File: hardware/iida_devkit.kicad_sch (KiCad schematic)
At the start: 45 parts, among them J1 PRPC005DAAN-RC, J2 Tag-Connect TC2050, J3 Conn_01x02, J4 USB4085-GF-A, U1 STM32L552CEU6, U2 MX25U4035FM1I, U3 MCP9808, U4 USBLC6-2SC6, Y1 ABS05-32.768KHZ-9-T, Y2 ECS-160-9-37-CKM-TR3

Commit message: Start working on hw v4.0.0
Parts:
- removed C1, C2, C3, C4: 8 pF, perfect_footprints:0402_1005_perfect, symbol Device:C
- removed C5, C8: 100 nF, perfect_footprints:0402_1005_perfect, symbol Device:C
- removed C6: 4.7 µF, Capacitor_SMD:C_0603_1608Metric, symbol Device:C
- removed C7: 33 pF, perfect_footprints:0402_1005_perfect, symbol Device:C
- removed F1: 5A, Fuse:Fuse_1812_4532Metric, symbol Device:Polyfuse
- removed J1: PRPC005DAAN-RC, Connector_PinHeader_2.54mm:PinHeader_2x05_P2.54mm_Vertical, symbol Connector_Generic:Conn_02x05_Odd_Even
- removed J2: Tag-Connect TC2050, Connector:Tag-Connect_TC2050-IDC-FP_2x05_P1.27mm_Vertical, symbol Connector:Conn_ARM_JTAG_SWD_10
- removed J3: Conn_01x02, Connector_PinHeader_2.54mm:PinHeader_1x02_P2.54mm_Vertical, symbol Connector_Generic:Conn_01x02
- removed J4: USB4085-GF-A, USB4105-GF-A:USB4085-GF-A, symbol USB4085-GF-A:USB4085-GF-A
- removed LED1, LED2, LED3, LED4: LS T67K-K1L2-1-0-2-R18-Z, LED_SMD:LED_PLCC_2835, symbol Device:LED
- removed R1, R2, R3, R4, R5, R6: 2.2 kΩ, perfect_footprints:0402_1005_perfect, symbol Device:R
- removed R10, R11, R12, R9: 0 Ω, perfect_footprints:0402_1005_perfect, symbol Device:R
- removed R13, R14: 5.1 kΩ, perfect_footprints:0402_1005_perfect, symbol Device:R
- removed R7, R8: 10 kΩ, perfect_footprints:0402_1005_perfect, symbol Device:R
- removed SW_SPST1: SW_RESET, Button_Switch_SMD:SW_SPST_PTS645, symbol Switch:SW_SPST
- removed U1: STM32L552CEU6, Package_DFN_QFN:QFN-48-1EP_7x7mm_P0.5mm_EP5.6x5.6mm, symbol MCU_ST_STM32L5:STM32L552CEUx
- removed U2: MX25U4035FM1I, Package_SO:SOIC-8_3.9x4.9mm_P1.27mm, symbol MX25U4035FM1I:MX25U4035FM1I
- removed U3: MCP9808, Package_SO:MSOP-8_3x3mm_P0.65mm, symbol Sensor_Temperature:MCP9808_MSOP
- removed U4: USBLC6-2SC6, Package_TO_SOT_SMD:SOT-23-6, symbol Power_Protection:USBLC6-2SC6
- removed Y1: ABS05-32.768KHZ-9-T, Crystal:Crystal_SMD_MicroCrystal_CM9V-T1A-2Pin_1.6x1.0mm, symbol Device:Crystal
- removed Y2: ECS-160-9-37-CKM-TR3, Crystal:Crystal_SMD_2016-4Pin_2.0x1.6mm, symbol Device:Crystal_GND24
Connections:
- no-connect marks 9 -> 0
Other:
- added sheet MCU (mcu.kicad_sch)
- note added: "Ext flash"
- note added: "Modem"
- note added: "POWER"
- note added: "SIM"
- note added: "Temp sensor"
- note removed: "16 MHz"
- note removed: "32.768 kHz"
- note removed: "Crystals"
- note removed: "Debug LEDs"
- note removed: "External flash"
- note removed: "Fiducial markers"
- note removed: "Hardware ID map"
- note removed: "Mounting holes"
- note removed: "NOTE: STM32F446RET6 has an internal pull-up resistor for D+"
- note removed: "Peripheral debug"
- note removed: "Programming header"
- note removed: "Reset"
- note removed: "Temperature sensor"
- note removed: "USB"
- note removed: "USBLC6-2 Datasheet: 1: D+ in 2: GND 3: D- in 4: D- out 5: VBUS 6: D+ out"
- note removed: "Wakeup"
- note removed: "With A0 .. A2 tied to ground, the address is 0b001'1000 (=0x18h)."

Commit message: HW: Develop further
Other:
- added sheet SIM (sim.kicad_sch)
- sheet MCU ports: added +3.3VA_MCU, +3.3V_MCU, MODEM_RX, MODEM_TX, ~{MODEM_PWR_EN}, ~{MODEM_RESET}; removed none
- sheet Modem ports: added +3.3V_MDM, MODEM_RX, MODEM_TX, SIM_CLK, SIM_IO, SIM_RST, VSIM, ~{MODEM_RESET}; removed none
- sheet Power ports: added +3.3VA_MCU, +3.3V_MCU, +3.3V_MDM, ~{MODEM_PWR_EN}; removed none
- note added: "Place fiducial markers at each (-1) corner of the PCB."
- note added: "Place mounting holes at the four corners of the PCB."
- note removed: "Ext flash"
- note removed: "MCU"
- note removed: "Modem"
- note removed: "POWER"
- note removed: "SIM"
- note removed: "Temp sensor"
- moved on the sheet: FID1, FID2, FID3, H1, H2, H3, H4

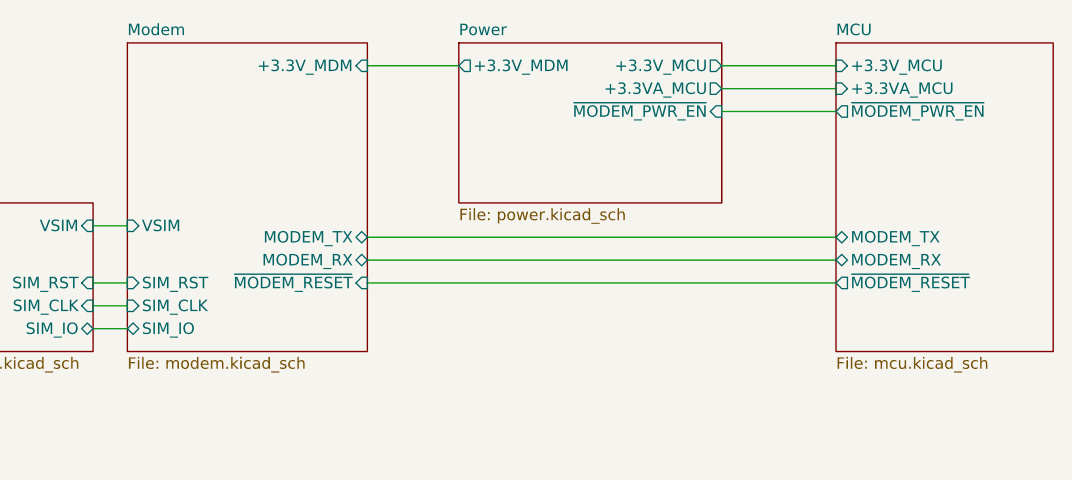
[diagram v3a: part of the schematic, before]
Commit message: HW: Rework power section
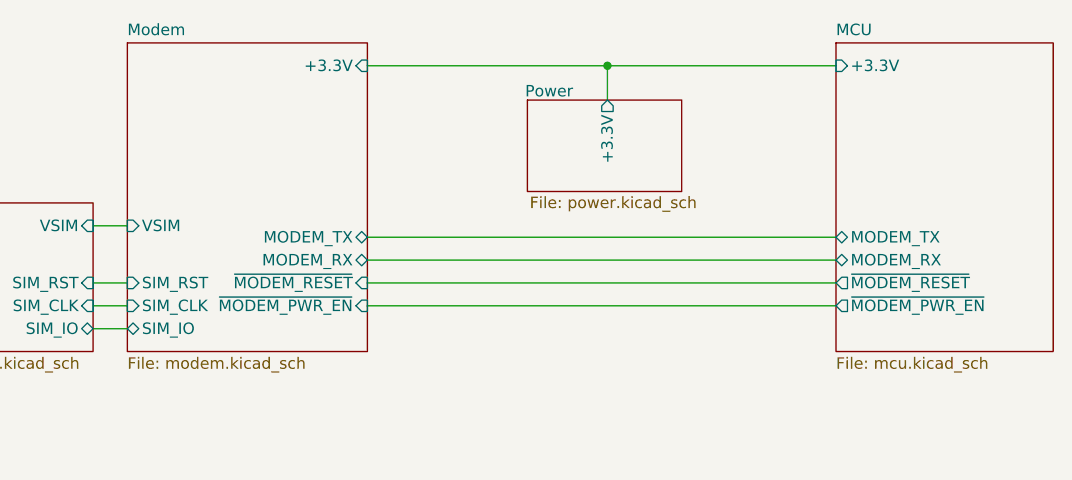
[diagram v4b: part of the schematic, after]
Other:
- sheet MCU ports: added +3.3V; removed +3.3VA_MCU, +3.3V_MCU
- sheet Modem ports: added +3.3V, ~{MODEM_PWR_EN}; removed +3.3V_MDM
- sheet Power ports: added +3.3V; removed +3.3VA_MCU, +3.3V_MCU, +3.3V_MDM, ~{MODEM_PWR_EN}
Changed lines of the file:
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@@
+	)
+	(junction
+		(at 152.4 83.82)
+		(diameter 0)
+		(color 0 0 0 0)
 	)
 	(junction
@@
 	(wire
 		(pts
+			(xy 152.4 83.82) (xy 152.4 87.63)
+		)
+		(stroke
+			(width 0)
+			(type default)
+		)
+	)
+	(wire
+		(pts
 			(xy 132.08 189.23) (xy 137.16 189.23)
 		)
@@
 	(wire
 		(pts
+			(xy 152.4 83.82) (xy 177.8 83.82)
+		)
+		(stroke
+			(width 0)
+			(type default)
+		)
+	)
+	(wire
+		(pts
 			(xy 137.16 189.23) (xy 142.24 189.23)
 		)
@@
 	(wire
 		(pts
+			(xy 125.73 83.82) (xy 152.4 83.82)
+		)
+		(stroke
+			(width 0)
+			(type default)
+		)
+	)
+	(wire
+		(pts
 			(xy 95.25 110.49) (xy 99.06 110.49)
 		)
@@
 	(wire
 		(pts
-			(xy 165.1 88.9) (xy 177.8 88.9)
-		)
-		(stroke
-			(width 0)
-			(type default)
-		)
-	)
-	(wire
-		(pts
-			(xy 165.1 83.82) (xy 177.8 83.82)
-		)
-		(stroke
-			(width 0)
-			(type default)
-		)
-	)
-	(wire
-		(pts
-			(xy 125.73 83.82) (xy 135.89 83.82)
+			(xy 125.73 110.49) (xy 177.8 110.49)
 		)
 		(stroke
@@
 		(pts
 			(xy 95.25 113.03) (xy 99.06 113.03)
-		)
-		(stroke
-			(width 0)
-			(type default)
-		)
-	)
-	(wire
-		(pts
-			(xy 165.1 86.36) (xy 177.8 86.36)
 		)
 		(stroke
@@
 			)
 		)
-		(pin "+3.3V_MDM" input
-			(at 125.73 83.82 0)
-			(effects
-				(font
-					(size 1.27 1.27)
-				)
-				(justify right)
-			)
-		)
 		(pin "SIM_IO" bidirectional
 			(at 99.06 113.03 180)
@@
 		(pin "MODEM_TX" bidirectional
 			(at 125.73 102.87 0)
+			(effects
+				(font
+					(size 1.27 1.27)
+				)
+				(justify right)
+			)
+		)
+		(pin "+3.3V" input
+			(at 125.73 83.82 0)
+			(effects
+				(font
+					(size 1.27 1.27)
+				)
+				(justify right)
+			)
+		)
+		(pin "~{MODEM_PWR_EN}" input
+			(at 125.73 110.49 0)
 			(effects
 				(font
@@
 			)
 		)
-		(pin "~{MODEM_PWR_EN}" output
-			(at 177.8 88.9 180)
-			(effects
-				(font
-					(size 1.27 1.27)
-				)
-				(justify left)
-			)
-		)
 		(pin "~{MODEM_RESET}" output
 			(at 177.8 107.95 180)
@@
 			)
 		)
-		(pin "+3.3V_MCU" input
+		(pin "+3.3V" input
 			(at 177.8 83.82 180)
 			(effects
@@
 			)
 		)
-		(pin "+3.3VA_MCU" input
-			(at 177.8 86.36 180)
+		(pin "~{MODEM_PWR_EN}" output
+			(at 177.8 110.49 180)
 			(effects
 				(font
@@
 	)
 	(sheet
-		(at 135.89 81.28)
-		(size 29.21 17.78)
-		(fields_autoplaced yes)
+		(at 143.51 87.63)
+		(size 17.145 10.16)
 		(stroke
 			(width 0.1524)
@@
 		)
 		(property "Sheetname" "Power"
-			(at 135.89 80.5684 0)
+			(at 143.256 87.376 0)
 			(effects
 				(font
@@
 		)
 		(property "Sheetfile" "power.kicad_sch"
-			(at 135.89 99.6446 0)
+			(at 143.764 98.298 0)
 			(effects
 				(font
@@
 			)
 		)
-		(pin "+3.3V_MDM" output
-			(at 135.89 83.82 180)
-			(effects
-				(font
-					(size 1.27 1.27)
-				)
-				(justify left)
-			)
-		)
-		(pin "~{MODEM_PWR_EN}" input
-			(at 165.1 88.9 0)
-			(effects
-				(font
-					(size 1.27 1.27)
-				)
-				(justify right)
-			)
-		)
-		(pin "+3.3V_MCU" output
-			(at 165.1 83.82 0)
-			(effects
-				(font
-					(size 1.27 1.27)
-				)
-				(justify right)
-			)
-		)
-		(pin "+3.3VA_MCU" output
-			(at 165.1 86.36 0)
-			(effects
-				(font
+		(pin "+3.3V" output
+			(at 152.4 87.63 90)
+			(effects
+				(font

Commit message: HW: Update schematic
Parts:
- H1, H2, H3, H4: footprint MountingHole:MountingHole_4.3mm_M4_Pad_Via -> MountingHole:MountingHole_2.2mm_M2_Pad_Via
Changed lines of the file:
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@@
 			)
 		)
-		(property "Footprint" "MountingHole:MountingHole_4.3mm_M4_Pad_Via"
+		(property "Footprint" "MountingHole:MountingHole_2.2mm_M2_Pad_Via"
 			(at 127 186.69 0)
 			(effects
@@
 			)
 		)
-		(property "Footprint" "MountingHole:MountingHole_4.3mm_M4_Pad_Via"
+		(property "Footprint" "MountingHole:MountingHole_2.2mm_M2_Pad_Via"
 			(at 142.24 186.69 0)
 			(effects
@@
 			)
 		)
-		(property "Footprint" "MountingHole:MountingHole_4.3mm_M4_Pad_Via"
+		(property "Footprint" "MountingHole:MountingHole_2.2mm_M2_Pad_Via"
 			(at 132.08 186.69 0)
 			(effects
@@
 			)
 		)
-		(property "Footprint" "MountingHole:MountingHole_4.3mm_M4_Pad_Via"
+		(property "Footprint" "MountingHole:MountingHole_2.2mm_M2_Pad_Via"
 			(at 137.16 186.69 0)
 			(effects

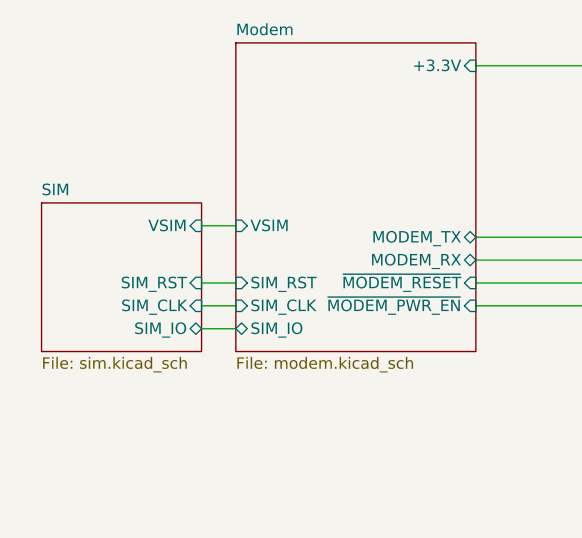
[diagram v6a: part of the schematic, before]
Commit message: HW: Add PCB antenna option
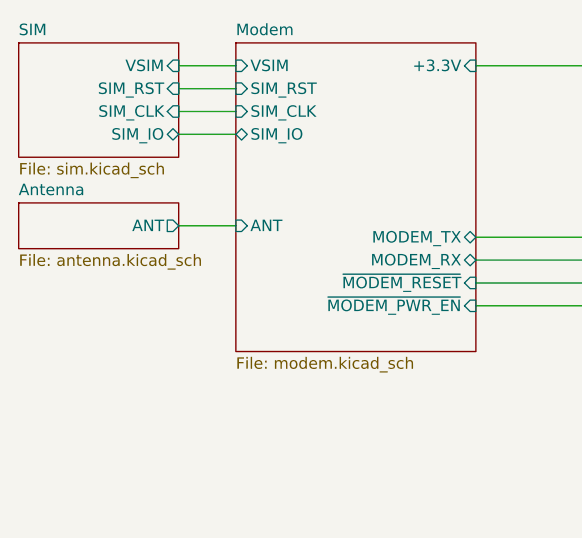
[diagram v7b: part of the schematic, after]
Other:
- added sheet Antenna (antenna.kicad_sch)
- sheet Modem ports: added ANT; removed none
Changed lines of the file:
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@@
 	(wire
 		(pts
-			(xy 95.25 101.6) (xy 99.06 101.6)
+			(xy 92.71 83.82) (xy 99.06 83.82)
 		)
 		(stroke
@@
 	(wire
 		(pts
-			(xy 95.25 107.95) (xy 99.06 107.95)
+			(xy 92.71 86.36) (xy 99.06 86.36)
 		)
 		(stroke
@@
 	(wire
 		(pts
-			(xy 95.25 110.49) (xy 99.06 110.49)
+			(xy 92.71 88.9) (xy 99.06 88.9)
 		)
 		(stroke
@@
 	(wire
 		(pts
-			(xy 95.25 113.03) (xy 99.06 113.03)
+			(xy 92.71 101.6) (xy 99.06 101.6)
+		)
+		(stroke
+			(width 0)
+			(type default)
+		)
+	)
+	(wire
+		(pts
+			(xy 92.71 91.44) (xy 99.06 91.44)
 		)
 		(stroke
@@
 	)
 	(sheet
-		(at 77.47 99.06)
-		(size 17.78 16.51)
+		(at 74.93 81.28)
+		(size 17.78 12.7)
 		(fields_autoplaced yes)
 		(stroke
@@
 		)
 		(property "Sheetname" "SIM"
-			(at 77.47 98.3484 0)
+			(at 74.93 80.5684 0)
 			(effects
 				(font
@@
 		)
 		(property "Sheetfile" "sim.kicad_sch"
-			(at 77.47 116.1546 0)
+			(at 74.93 94.5646 0)
 			(effects
 				(font
@@
 		)
 		(pin "SIM_RST" input
-			(at 95.25 107.95 0)
+			(at 92.71 86.36 0)
 			(effects
 				(font
@@
 		)
 		(pin "VSIM" input
-			(at 95.25 101.6 0)
+			(at 92.71 83.82 0)
 			(effects
 				(font
@@
 		)
 		(pin "SIM_CLK" input
-			(at 95.25 110.49 0)
+			(at 92.71 88.9 0)
 			(effects
 				(font
@@
 		)
 		(pin "SIM_IO" bidirectional
-			(at 95.25 113.03 0)
+			(at 92.71 91.44 0)
 			(effects
 				(font
@@
 		)
 		(pin "SIM_IO" bidirectional
-			(at 99.06 113.03 180)
+			(at 99.06 91.44 180)
 			(effects
 				(font
@@
 		)
 		(pin "VSIM" input
-			(at 99.06 101.6 180)
+			(at 99.06 83.82 180)
 			(effects
 				(font
@@
 		)
 		(pin "SIM_RST" input
-			(at 99.06 107.95 180)
+			(at 99.06 86.36 180)
 			(effects
 				(font
@@
 		)
 		(pin "SIM_CLK" input
-			(at 99.06 110.49 180)
+			(at 99.06 88.9 180)
 			(effects
 				(font
@@
 				)
 				(justify right)
+			)
+		)
+		(pin "ANT" input
+			(at 99.06 101.6 180)
+			(effects
+				(font
+					(size 1.27 1.27)
+				)
+				(justify left)
 			)
 		)
@@
 				)
 			)
+		)
+	)
+	(sheet
+		(at 74.93 99.06)
+		(size 17.78 5.08)
+		(fields_autoplaced yes)
+		(stroke
+			(width 0.1524)
+			(type solid)
+			(color 0 0 0 1)
+		)
+		(fill
+			(color 0 255 0 1.0000)
+		)
+		(property "Sheetname" "Antenna"
+			(at 74.93 98.3484 0)
+			(effects
+				(font
+					(size 1.27 1.27)
+				)
+				(justify left bottom)
+			)
+		)
+		(property "Sheetfile" "antenna.kicad_sch"
+			(at 74.93 104.7246 0)
+			(effects
+				(font
+					(size 1.27 1.27)
+				)
+				(justify left top)
+			)
+		)
+		(pin "ANT" output
+			(at 92.71 101.6 0)
+			(effects
+				(font
+					(size 1.27 1.27)
+				)
+				(justify right)
+			)
+		)
+		(instances
+			(project "iida_devkit"
+				(path "/b12a6e25-97fb-4aba-bc96-af8db389bb9a"
+					(page "6")
+				)
+			)

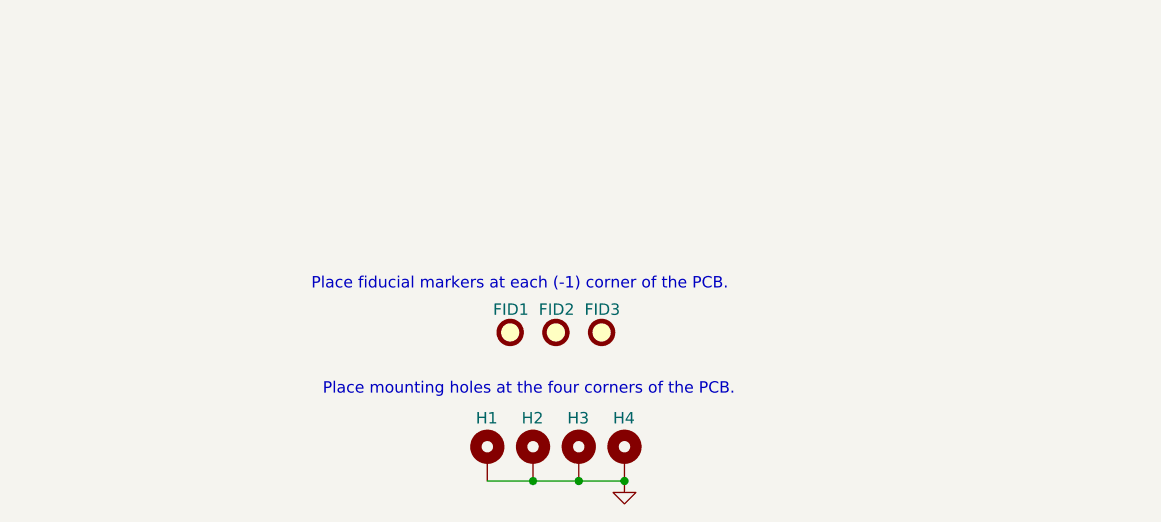
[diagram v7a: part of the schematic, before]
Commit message: HW: Add layout guidelines/reminders to schematic
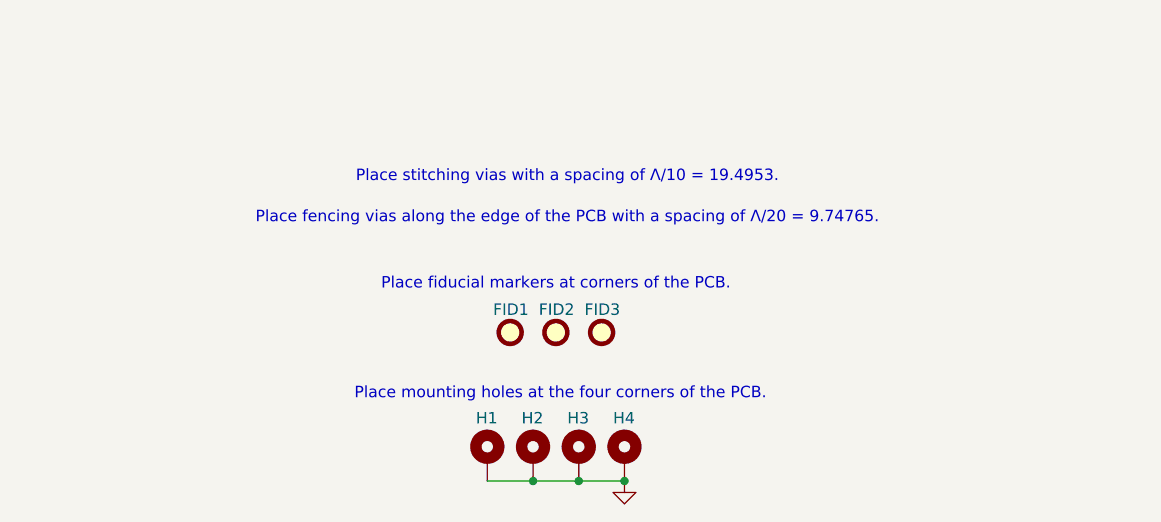
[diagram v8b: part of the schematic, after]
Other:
- note added: "Place fencing vias along the edge of the PCB with a spacing of Λ/20 = 9.74765."
- note added: "Place fiducial markers at corners of the PCB."
- note added: "Place stitching vias with a spacing of Λ/10 = 19.4953."
- note removed: "Place fiducial markers at each (-1) corner of the PCB."
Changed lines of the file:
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@@
 		)
 	)
-	(text "Place fiducial markers at each (-1) corner of the PCB."
+	(text "Place stitching vias with a spacing of Λ/10 = 19.4953."
 		(exclude_from_sim no)
-		(at 107.442 167.386 0)
+		(at 135.89 155.448 0)
 		(effects
 			(font
 				(size 1.27 1.27)
 			)
-			(justify left)
+		)
+	)
+	(text "Place fencing vias along the edge of the PCB with a spacing of Λ/20 = 9.74765."
+		(exclude_from_sim no)
+		(at 135.89 160.02 0)
+		(effects
+			(font
+				(size 1.27 1.27)
+			)
+		)
+	)
+	(text "Place fiducial markers at corners of the PCB."
+		(exclude_from_sim no)
+		(at 134.62 167.386 0)
+		(effects
+			(font
+				(size 1.27 1.27)
+			)
 		)
 	)
 	(text "Place mounting holes at the four corners of the PCB."
 		(exclude_from_sim no)
-		(at 108.712 179.07 0)
+		(at 135.128 179.578 0)
 		(effects
 			(font
 				(size 1.27 1.27)
 			)
-			(justify left)
 		)
 	)
